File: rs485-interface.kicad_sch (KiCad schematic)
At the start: 9 parts, among them Q1 Q_PMOS_GSD, Q2 Q_NMOS_GSD, U1 SN65HVD72

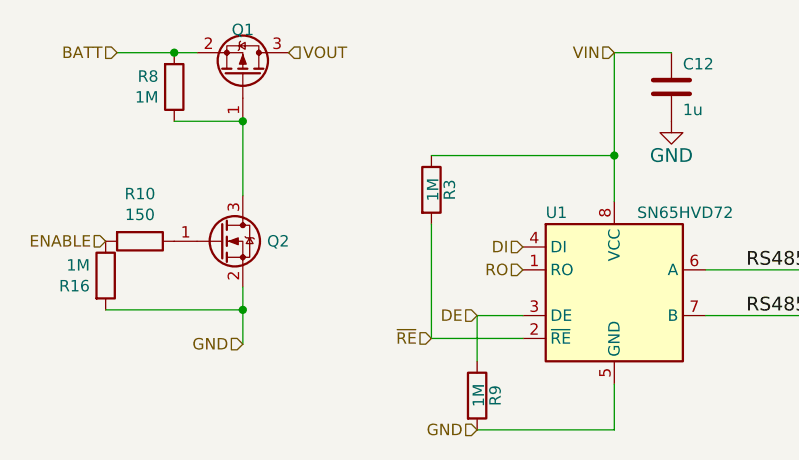
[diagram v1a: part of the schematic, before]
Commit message: New kicad formats. Mark holes and fiducials and other DNP components as non-bom, update values for transistors and diodes
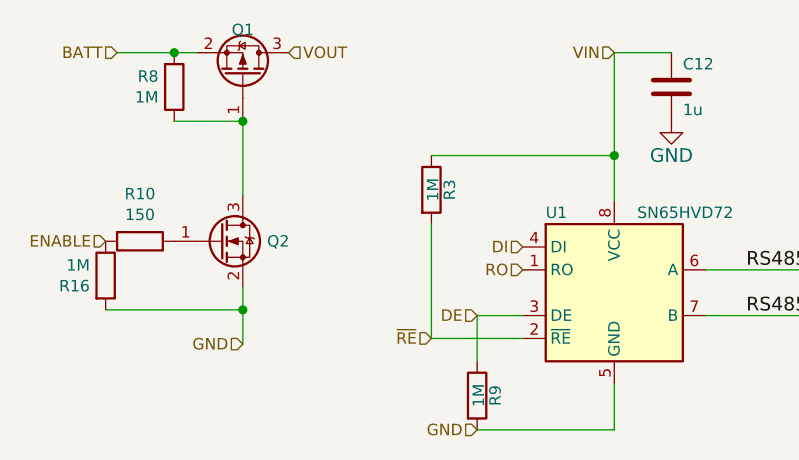
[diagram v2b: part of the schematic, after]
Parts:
- Q1: value Q_PMOS_GSD -> NX2301P
- Q2: value Q_NMOS_GSD -> NTR4003
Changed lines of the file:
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@@
-(kicad_sch (version 20200512) (host eeschema "5.99.0-unknown-eae0c14~88~ubuntu18.04.1")
-  (page 1 5)
+(kicad_sch (version 20200828) (generator eeschema)
+  (page 4 5)
   (paper "A4")
-  (junction (at 46.99 31.75))
-  (junction (at 54.61 39.37))
-  (junction (at 54.61 60.325))
-  (junction (at 95.885 43.18))
+  (junction (at 46.99 31.75) (diameter 1.016) (color 0 0 0 0))
+  (junction (at 54.61 39.37) (diameter 1.016) (color 0 0 0 0))
+  (junction (at 54.61 60.325) (diameter 1.016) (color 0 0 0 0))
+  (junction (at 95.885 43.18) (diameter 1.016) (color 0 0 0 0))
   (wire (pts (xy 39.37 60.325) (xy 54.61 60.325))
     (stroke (width 0) (type solid) (color 0 0 0 0))
@@
   )
   (symbol (lib_id "power:GND") (at 102.235 39.37 0) (unit 1)
+    (in_bom yes) (on_board yes)
     (property "Reference" "#PWR018" (id 0) (at 102.235 45.72 0)
       (effects (font (size 1.524 1.524)) hide)
@@
   )
   (symbol (lib_id "Device:R") (at 39.37 56.515 0) (unit 1)
+    (in_bom yes) (on_board yes)
     (property "Reference" "R16" (id 0) (at 37.6174 57.6834 0)
       (effects (font (size 1.27 1.27)) (justify right))
@@
   )
   (symbol (lib_id "Device:R") (at 43.18 52.705 270) (unit 1)
+    (in_bom yes) (on_board yes)
     (property "Reference" "R10" (id 0) (at 43.18 47.4472 90))
     (property "Value" "150" (id 1) (at 43.18 49.7586 90))
@@
   )
   (symbol (lib_id "Device:R") (at 46.99 35.56 0) (mirror x) (unit 1)
+    (in_bom yes) (on_board yes)
     (property "Reference" "R8" (id 0) (at 45.2374 34.3916 0)
       (effects (font (size 1.27 1.27)) (justify right))
@@
   )
   (symbol (lib_id "Device:R") (at 75.565 46.99 0) (unit 1)
+    (in_bom yes) (on_board yes)
     (property "Reference" "R3" (id 0) (at 77.597 46.99 90))
     (property "Value" "1M" (id 1) (at 75.7428 46.9646 90))
@@
   )
   (symbol (lib_id "Device:R") (at 80.645 69.85 0) (unit 1)
+    (in_bom yes) (on_board yes)
     (property "Reference" "R9" (id 0) (at 82.677 69.85 90))
     (property "Value" "1M" (id 1) (at 80.8228 69.8246 90))
@@
   )
   (symbol (lib_id "Device:C") (at 102.235 35.56 0) (unit 1)
+    (in_bom yes) (on_board yes)
     (property "Reference" "C12" (id 0) (at 103.505 33.02 0)
       (effects (font (size 1.27 1.27)) (justify left))
@@
   )
   (symbol (lib_id "Device:Q_NMOS_GSD") (at 52.07 52.705 0) (unit 1)
+    (in_bom yes) (on_board yes)
     (property "Reference" "Q2" (id 0) (at 57.3024 52.705 0)
       (effects (font (size 1.27 1.27)) (justify left))
     )
-    (property "Value" "Q_NMOS_GSD" (id 1) (at 57.3024 53.848 0)
+    (property "Value" "NTR4003" (id 1) (at 57.3024 53.848 0)
       (effects (font (size 1.27 1.27)) (justify left) hide)
     )
@@
   )
   (symbol (lib_id "Device:Q_PMOS_GSD") (at 54.61 34.29 270) (mirror x) (unit 1)
+    (in_bom yes) (on_board yes)
     (property "Reference" "Q1" (id 0) (at 54.61 29.21 90))
-    (property "Value" "Q_PMOS_GSD" (id 1) (at 54.61 28.2702 90)
+    (property "Value" "NX2301P" (id 1) (at 54.61 28.2702 90)
       (effects (font (size 1.27 1.27)) hide)
     )
@@
   )
   (symbol (lib_id "miceuz:SN65HVD") (at 95.885 58.42 0) (unit 1)
+    (in_bom yes) (on_board yes)
     (property "Reference" "U1" (id 0) (at 88.265 49.53 0)
       (effects (font (size 1.27 1.27)) (justify left))

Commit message: Update PCB:  * Update shape so it fits into case  * Update most of the components for JLCPCB assembly
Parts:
- C12: LCSC (none) -> C15849
- Q1: LCSC (none) -> C10487
- Q2: LCSC (none) -> C8545
- R10: LCSC (none) -> C22808
- R16, R3, R8, R9: LCSC (none) -> C22935
- U1: LCSC (none) -> C48125
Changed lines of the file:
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@@
-(kicad_sch (version 20200828) (generator eeschema)
-  (page 4 5)
+(kicad_sch (version 20201015) (generator eeschema)
+  (page 1 5)
   (paper "A4")
   (junction (at 46.99 31.75) (diameter 1.016) (color 0 0 0 0))
@@
       (effects (font (size 1.27 1.27)) hide)
     )
+    (property "LCSC" "C22935" (id 4) (at 39.37 56.515 0)
+      (effects (font (size 1.27 1.27)) hide)
+    )
   )
   (symbol (lib_id "Device:R") (at 43.18 52.705 270) (unit 1)
@@
       (effects (font (size 1.27 1.27)) hide)
     )
+    (property "LCSC" "C22808" (id 4) (at 43.18 52.705 0)
+      (effects (font (size 1.27 1.27)) hide)
+    )
   )
   (symbol (lib_id "Device:R") (at 46.99 35.56 0) (mirror x) (unit 1)
@@
     )
     (property "Datasheet" "~" (id 3) (at 46.99 35.56 0)
+      (effects (font (size 1.27 1.27)) hide)
+    )
+    (property "LCSC" "C22935" (id 4) (at 46.99 35.56 0)
       (effects (font (size 1.27 1.27)) hide)
     )
@@
       (effects (font (size 1.27 1.27)) hide)
     )
+    (property "LCSC" "C22935" (id 4) (at 75.565 46.99 0)
+      (effects (font (size 1.27 1.27)) hide)
+    )
   )
   (symbol (lib_id "Device:R") (at 80.645 69.85 0) (unit 1)
@@
       (effects (font (size 1.27 1.27)) hide)
     )
+    (property "LCSC" "C22935" (id 4) (at 80.645 69.85 0)
+      (effects (font (size 1.27 1.27)) hide)
+    )
   )
   (symbol (lib_id "Device:C") (at 102.235 35.56 0) (unit 1)
@@
       (effects (font (size 1.27 1.27)) hide)
     )
+    (property "LCSC" "C15849" (id 4) (at 102.235 35.56 0)
+      (effects (font (size 1.27 1.27)) hide)
+    )
   )
   (symbol (lib_id "Device:Q_NMOS_GSD") (at 52.07 52.705 0) (unit 1)
@@
       (effects (font (size 1.27 1.27)) hide)
     )
+    (property "LCSC" "C8545" (id 4) (at 52.07 52.705 0)
+      (effects (font (size 1.27 1.27)) hide)
+    )
   )
   (symbol (lib_id "Device:Q_PMOS_GSD") (at 54.61 34.29 270) (mirror x) (unit 1)
@@
       (effects (font (size 1.27 1.27)) hide)
     )
+    (property "LCSC" "C10487" (id 4) (at 54.61 34.29 0)
+      (effects (font (size 1.27 1.27)) hide)
+    )
   )
   (symbol (lib_id "miceuz:SN65HVD") (at 95.885 58.42 0) (unit 1)
@@
       (effects (font (size 1.524 1.524)) hide)
     )
-  )
+    (property "LCSC" "C48125" (id 4) (at 95.885 58.42 0)
+      (effects (font (size 1.27 1.27)) hide)
+    )
+  )

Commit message: Fix ESD diode symbol and routing. Update reset/boot0 circuit to one that works satisfactory
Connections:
- net ~RE renamed ~{RE}

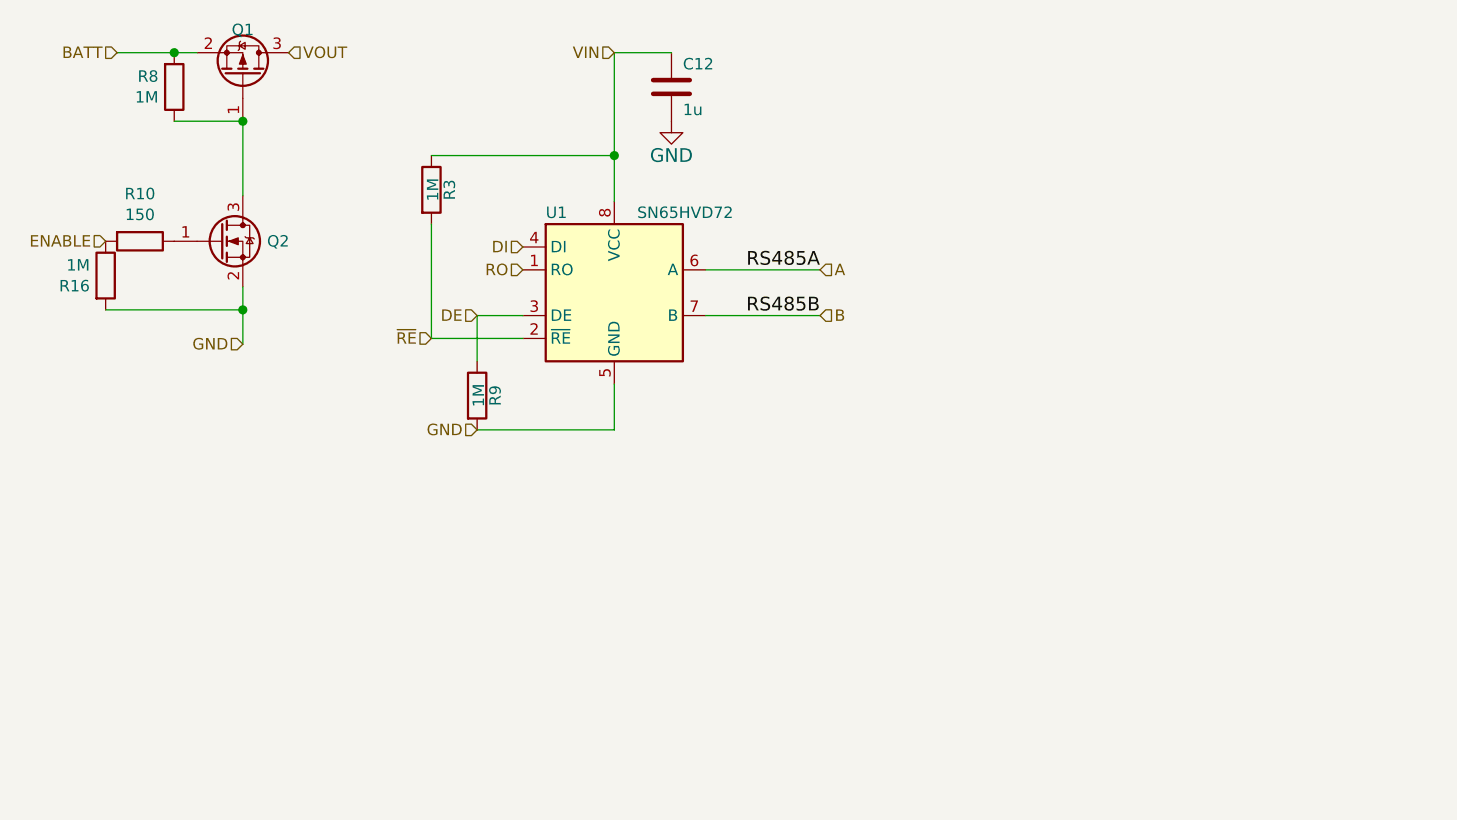
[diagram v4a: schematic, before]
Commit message: Set proper LCSC numbers to components, consolidate some values
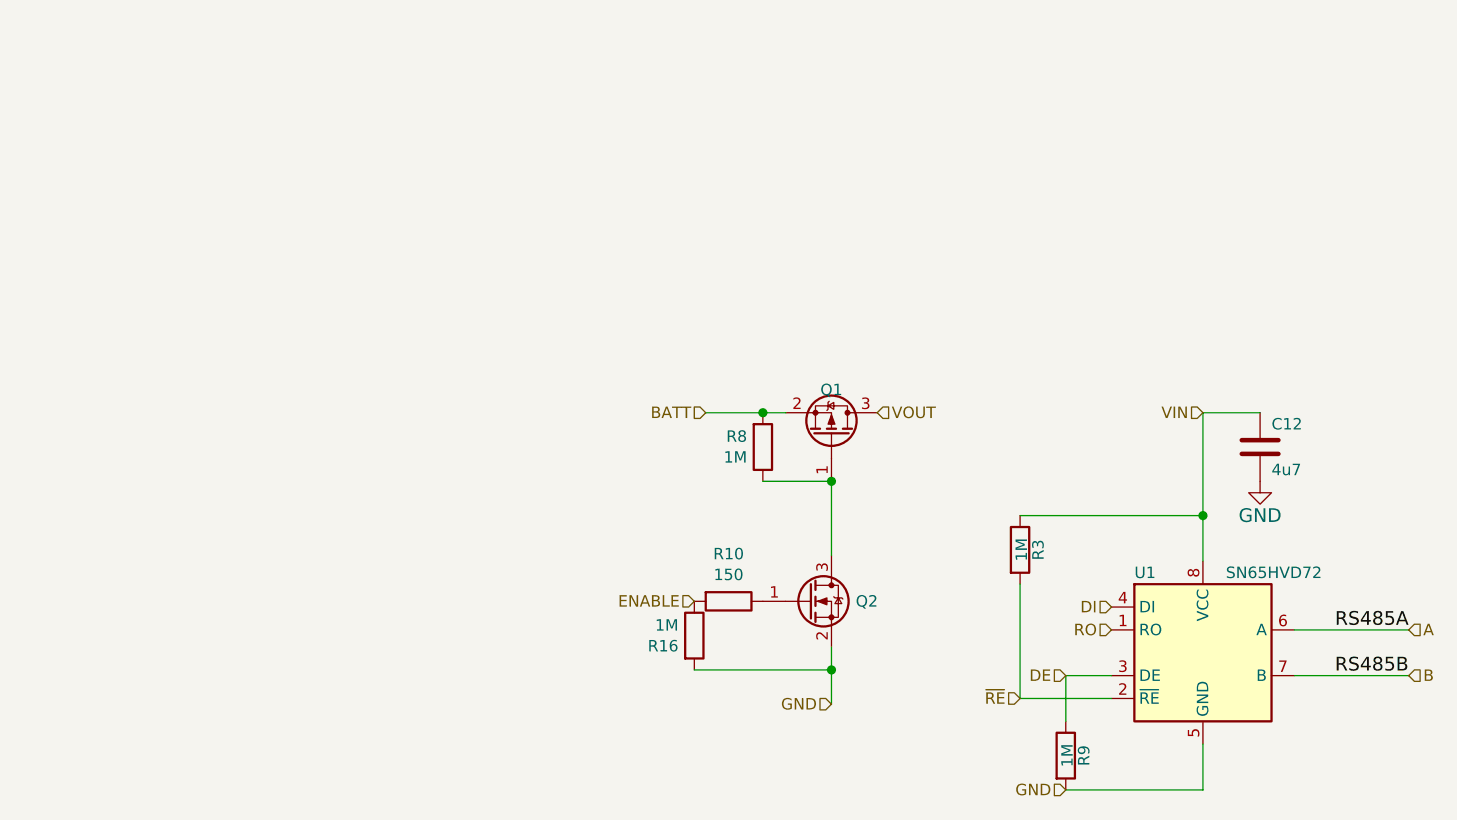
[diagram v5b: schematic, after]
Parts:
- C12: value 1u -> 4u7; LCSC C15849 -> C19666
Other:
- moved on the sheet: C12, Q1, Q2, R10, R16, R3, R8, R9, U1
